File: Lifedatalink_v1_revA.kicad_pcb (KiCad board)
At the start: 2 copper layers, 127.5 x 74.7 mm, 94 parts, among them J1 DX07S024XJ1R1100, J10 503480-0400, J11 5034801400, J12 5034801400, J13 503480-0600, J14 503480-0600, J15 503480-0600, J16 503480-0600, J17 503480-0600, J18 503480-0600, J19 503480-0600, J2 BATTERY CONNECTOR, J20 503480-0600, J3 Conn_02x10_Odd_Even, J4 Conn_01x06, J5 503480-0400, J6 503480-0400, J7 503480-0400, J8 503480-0400, J9 503480-0400, Q1 DMG2301L, U1 BL654, U2 LP5907MFX-3_3_NOPB, U3 ADS1292R, U4 MCP73831-2-OT, U5 TMP117NAIYBGR, U6 MAX30102, U7 LP5907MFX-1.8, U8 IIS2DLPCTR, U9 PCA9306, Y1 Crystal

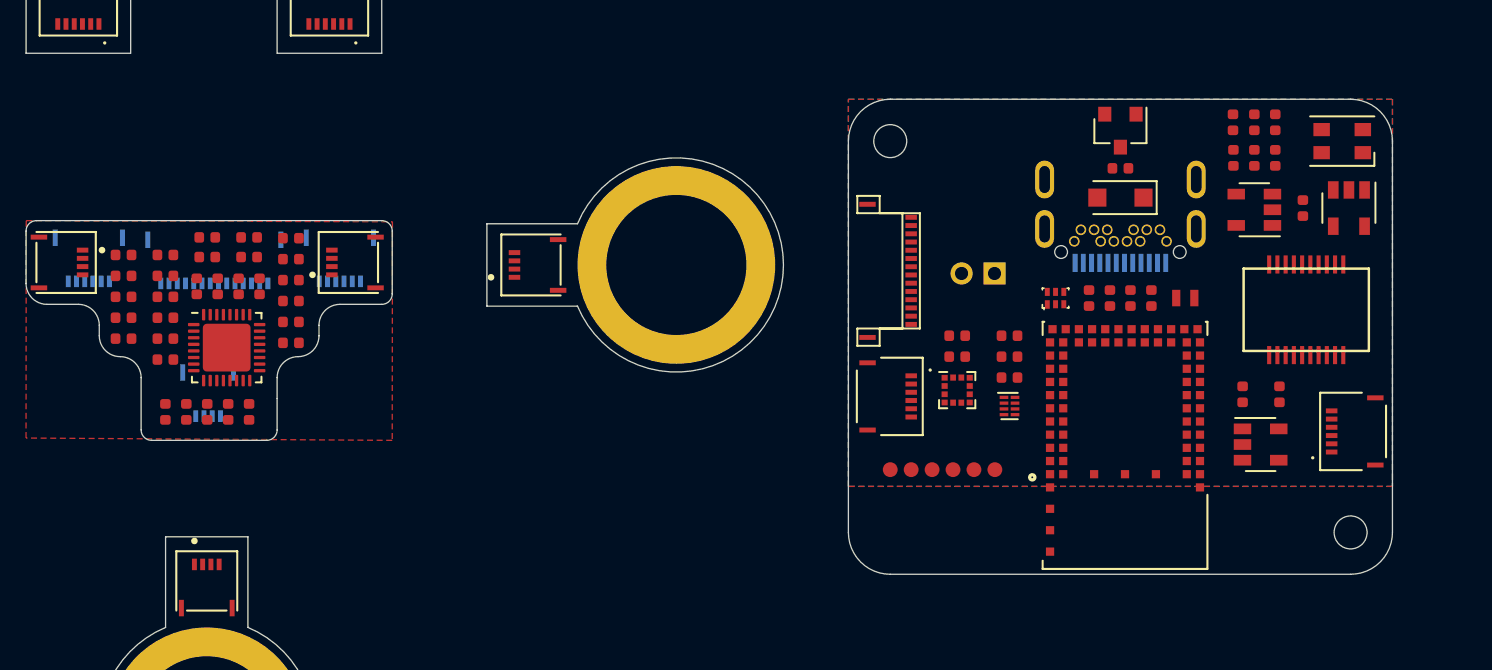
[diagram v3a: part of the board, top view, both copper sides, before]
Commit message: Fixed LED and added JST connector to battery plus more 3D models
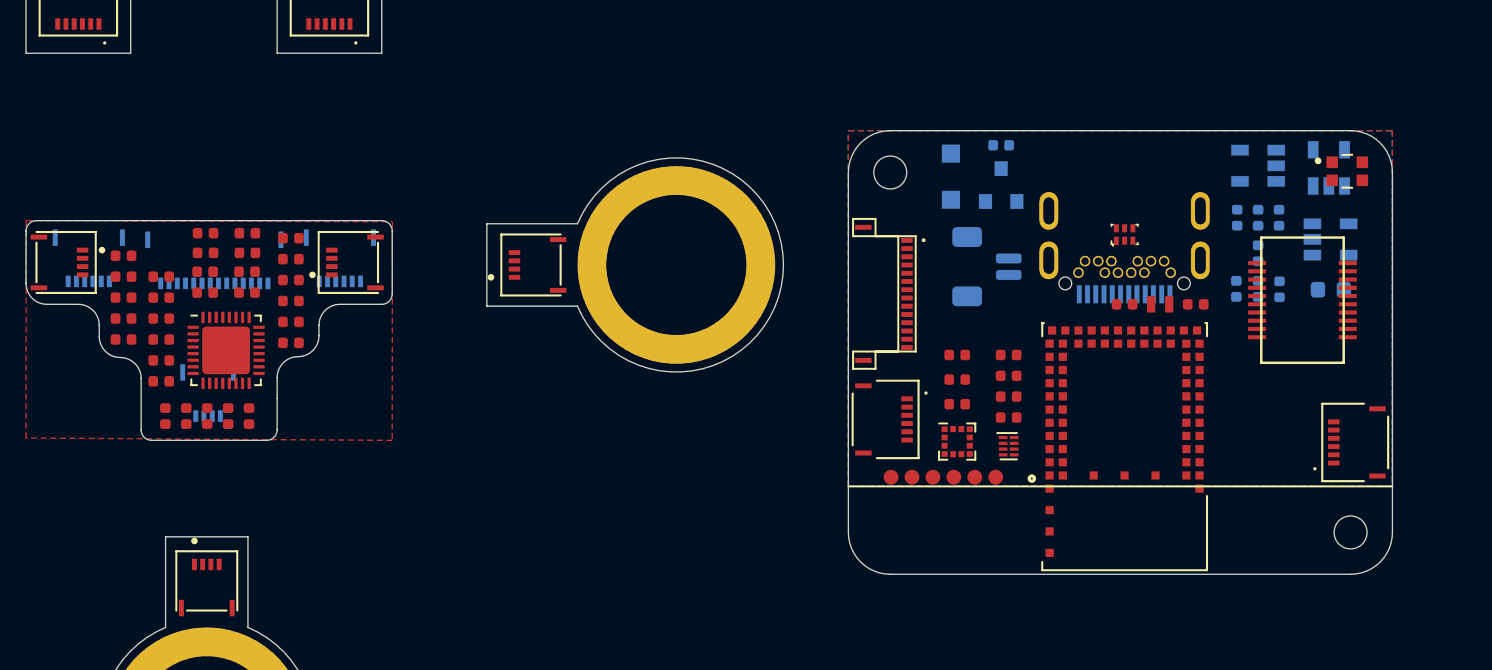
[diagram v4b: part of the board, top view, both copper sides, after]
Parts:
- removed R1, R2: 470, Resistor_SMD:R_0402_1005Metric
- added F1: 0603L075SLYR, Fuse:Fuse_0603_1608Metric, B.Cu at (192.2, 135.0)
- C25, C26, C3, C4, C6, C7, D3, Q1, R3, R4, U2, U4, U7: moved to B.Cu
- D2: value LTST-C155KGJRKT -> WS2812B; footprint SeeedOPL-LED:LED_Cree-PLCC4_3.2x2.8mm_CCW_jose -> APA-102-2020-256-8:LED_WS2812-2020
- J2: footprint Connector_PinHeader_2.00mm:PinHeader_1x02_P2.00mm_Vertical -> Connector_JST:JST_SH_BM02B-SRSS-TB_1x02-1MP_P1.00mm_Vertical
- moved U7 13.1 mm to (192.2, 132.0)
- moved D3 10.4 mm to (169.2, 128.1), turned to 270 degrees
- moved R19 10.3 mm to (169.5, 141.9), turned to 0 degrees
- moved R18 9.50 mm to (172.7, 142.8), turned to 0 degrees
- moved C7 8.09 mm to (187.8, 132.8), turned to 270 degrees
- moved Q1 7.96 mm to (172.2, 128.7), turned to 90 degrees
- moved R4 7.37 mm to (172.2, 126.2)
- moved C26 6.91 mm to (186.5, 135.0), turned to 90 degrees
- moved C25 6.47 mm to (187.8, 135.0), turned to 90 degrees
- moved D1 5.70 mm to (179.7, 131.6)
- moved R3 5.13 mm to (189.1, 135.0)
- moved C3 3.64 mm to (187.8, 130.6), turned to 270 degrees
- moved C4 3.64 mm to (186.5, 130.6), turned to 270 degrees
- moved C6 3.64 mm to (189.1, 130.6), turned to 270 degrees
- moved U8 3.12 mm to (169.5, 144.2)
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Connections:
- D2 pad 2: +5V -> GND
- D2 pad 3: GND -> /WS2812_DATA
- D2 pad 4: Net-(D2-Pad4) -> /VIN
- J4 pad 1: +3V3 -> Net-(J4-Pad1)
- U1 pad 6: Net-(U1-Pad6) -> /MCP73831_STAT
- U1 pad 63: Net-(U1-Pad63) -> /WS2812_DATA
- U2 pad 1: Net-(C3-Pad2) -> Net-(F1-Pad1)
- U2 pad 3: Net-(C3-Pad2) -> Net-(F1-Pad1)
- U4 pad 1: Net-(R1-Pad2) -> /MCP73831_STAT
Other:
- outline, holes or cut-outs redrawn

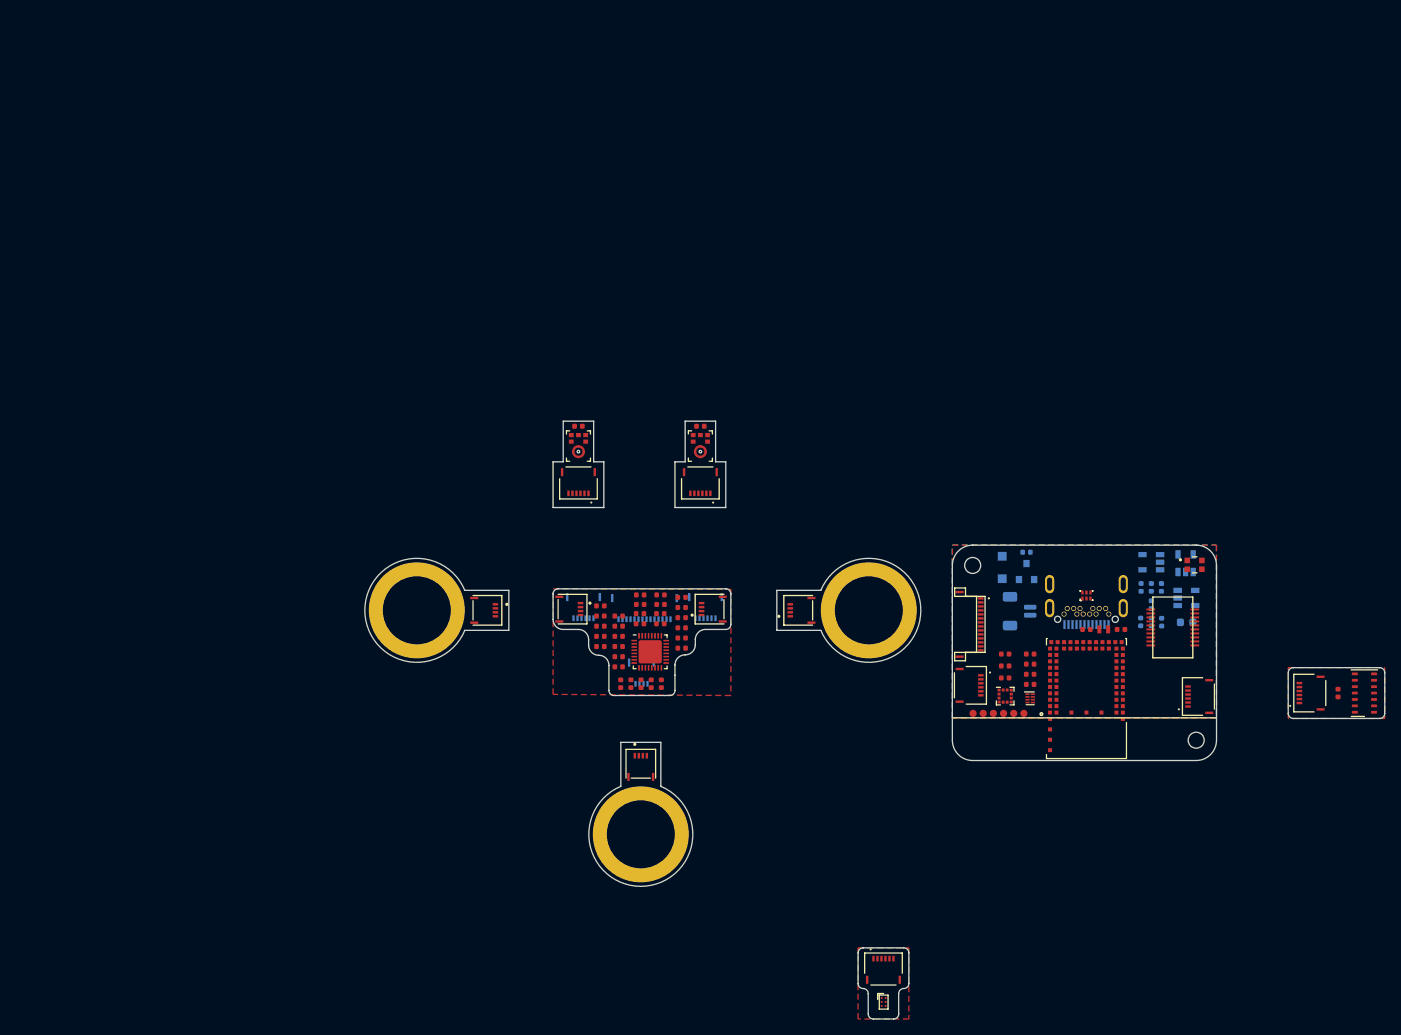
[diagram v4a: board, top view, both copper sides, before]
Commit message: Changed layout and added button
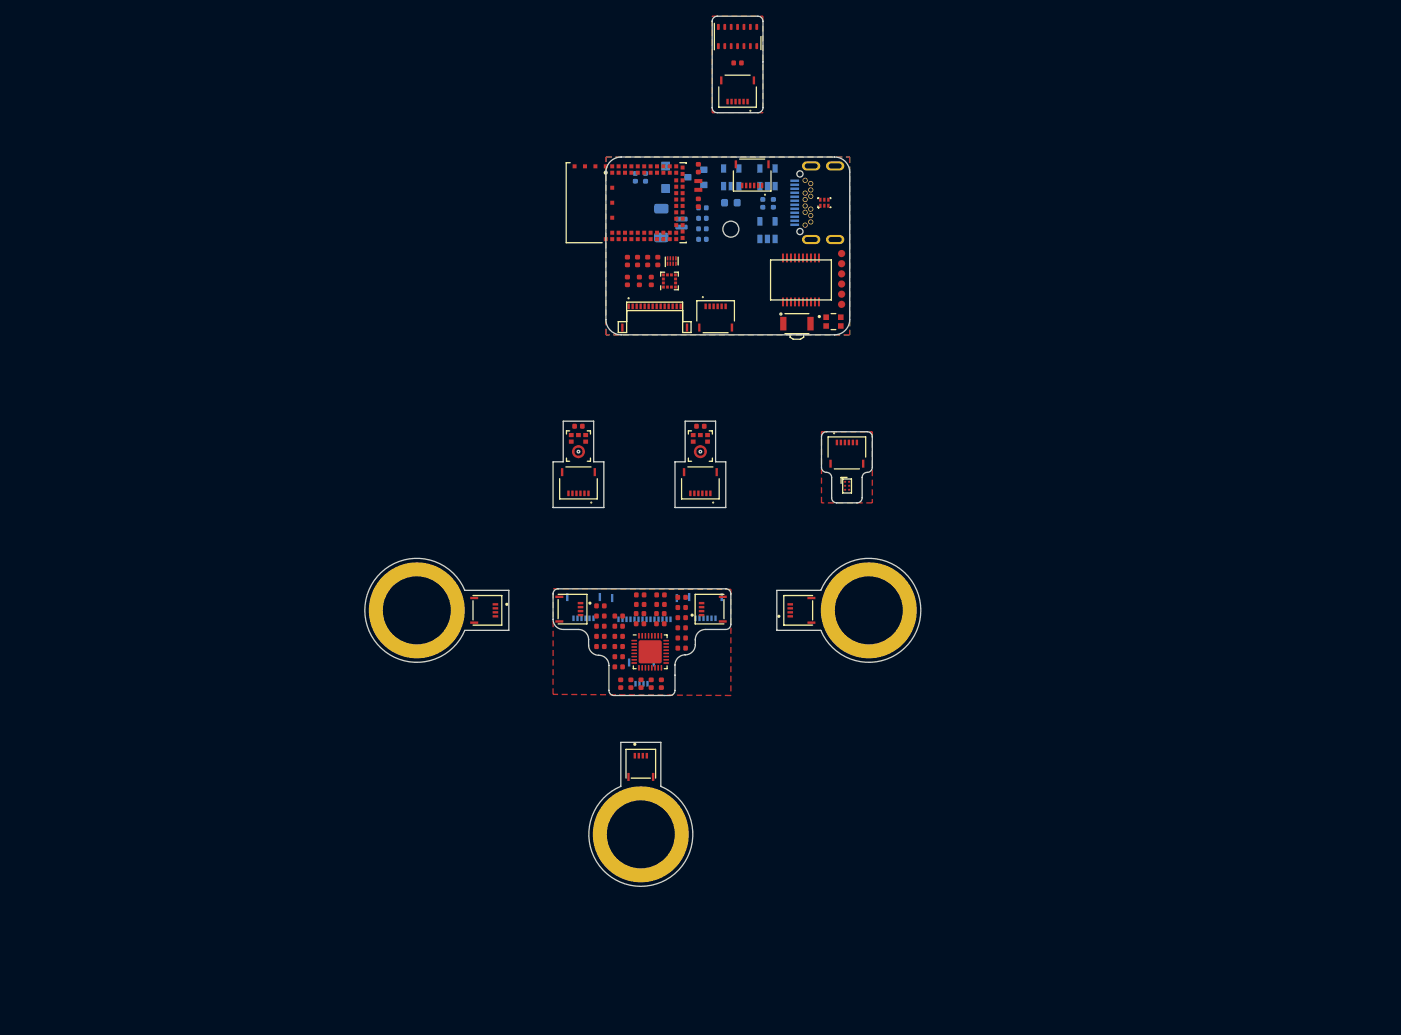
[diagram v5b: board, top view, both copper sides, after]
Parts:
- removed the REF** at (165.5, 127.9)
- added SW1: SW_Push, SW_B3U-3000P:SW_B3U-3000P, F.Cu at (143.5, 97.7)
- REF**: moved to B.Cu
- moved U6 113.5 mm to (136.1, 61.8), turned to 270 degrees
- moved C24 108.8 mm to (136.1, 65.1), turned to 180 degrees
- moved J16 104.0 mm to (136.1, 68.5), turned to 180 degrees
- moved REF** 86.4 mm to (135.3, 85.9)
- moved J15 85.9 mm to (137.9, 79.0), turned to 180 degrees
- moved U1 84.6 mm to (122.2, 82.5), turned to 90 degrees
- moved C3 82.4 mm to (123.3, 79.4)
- moved C2 78.2 mm to (131.2, 78.2), turned to 90 degrees
- moved F1 77.4 mm to (135.3, 82.5), turned to 0 degrees
- moved R3 76.4 mm to (131.7, 84.5), turned to 0 degrees
- moved Y1 75.2 mm to (131.2, 80.4), turned to 90 degrees
- moved C7 74.9 mm to (131.7, 83.2), turned to 180 degrees
- moved C1 72.1 mm to (131.2, 82.5), turned to 90 degrees
- moved C6 72.0 mm to (131.7, 87.1), turned to 180 degrees
- moved U2 71.2 mm to (135.3, 79.4), turned to 90 degrees
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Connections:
- U1 pad 2: Net-(U1-Pad2) -> /WS2812_DATA
- U1 pad 6: /MCP73831_STAT -> Net-(SW1-Pad1)
- U1 pad 63: /WS2812_DATA -> /MCP73831_STAT
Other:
- board size 127.5 x 74.7 mm -> 69.5 x 108.8 mm

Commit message: Added board properties
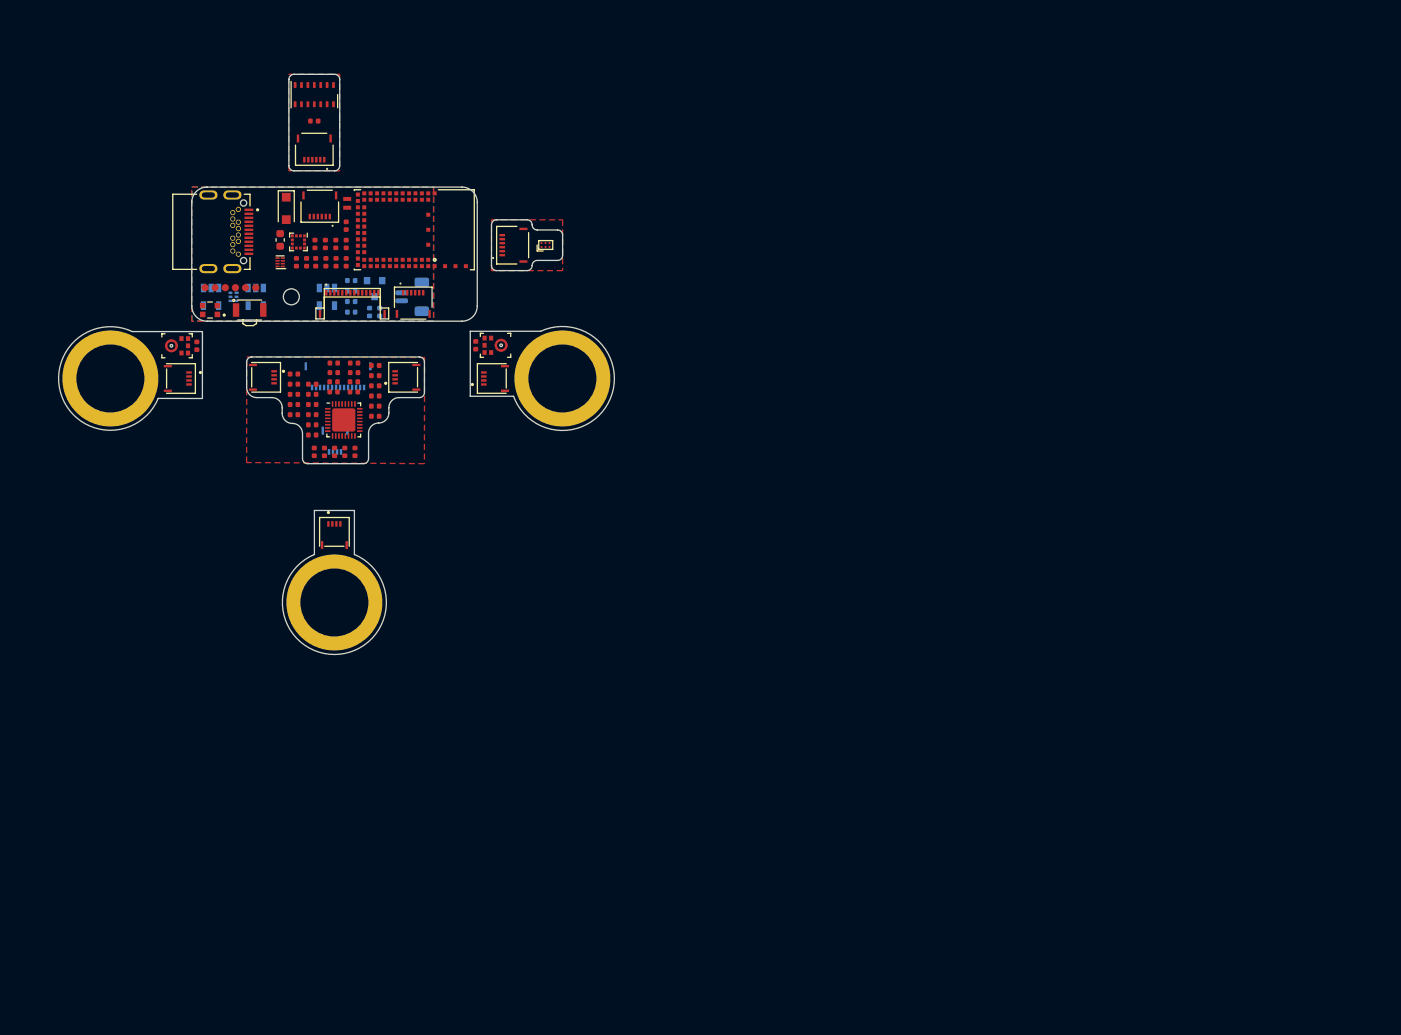
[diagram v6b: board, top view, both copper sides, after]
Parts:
- removed J17, J18, J19, J20: 503480-0600, MOLEX_503480-0600:MOLEX_503480-0600
- removed J3: Conn_02x10_Odd_Even, DF23:DF23C-20DS-0.5V(51)
- C25, C26, D3, F1, J1: moved to F.Cu
- D1: moved to B.Cu
- moved D2 77.9 mm to (70.2, 96.0), turned to 180 degrees
- moved J4 76.4 mm to (72.7, 93.2), turned to 0 degrees
- moved D1 74.8 mm to (73.1, 94.3), turned to 270 degrees
- moved J1 69.6 mm to (74.3, 86.2)
- moved SW1 68.4 mm to (75.1, 96.0)
- moved U2 66.7 mm to (70.3, 94.3), turned to 270 degrees
- moved U4 65.7 mm to (75.9, 94.3), turned to 270 degrees
- moved F1 56.5 mm to (78.9, 87.2), turned to 90 degrees
- moved U7 55.7 mm to (84.8, 94.3), turned to 270 degrees
- moved REF** 55.6 mm to (80.3, 94.3), turned to 180 degrees
- moved C25 55.2 mm to (85.9, 90.0)
- moved J15 54.2 mm to (83.9, 82.9)
- moved C24 53.4 mm to (83.2, 72.3)
- moved J16 53.4 mm to (83.2, 75.8)
- moved U6 53.4 mm to (83.2, 69.0)
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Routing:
- added copper zone on In2.Cu, net +3V3
- added copper zone on In1.Cu, net GND
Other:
- board size 69.5 x 108.8 mm -> 69.5 x 72.5 mm
- copper layers 2 -> 4
- net class Default: clearance 0.2 -> 0.1524; trace_width 0.25 -> 0.1524; via_dia 0.8 -> 0.6; via_drill 0.4 -> 0.3
- net class Power added: clearance 0.2, trace_width 0.25, via_dia 0.8, via_drill 0.4
- rule trace_clearance: 0.2 -> 0.1524
- rule trace_min: 0.2 -> 0.1524
- rule via_min_drill: 0.3 -> 0.2
- rule via_min_size: 0.4 -> 0.35
